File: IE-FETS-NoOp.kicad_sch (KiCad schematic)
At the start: 12 parts, among them Q1 YJG150N03A, Q4 YJG150N03A, U4 INA185A1

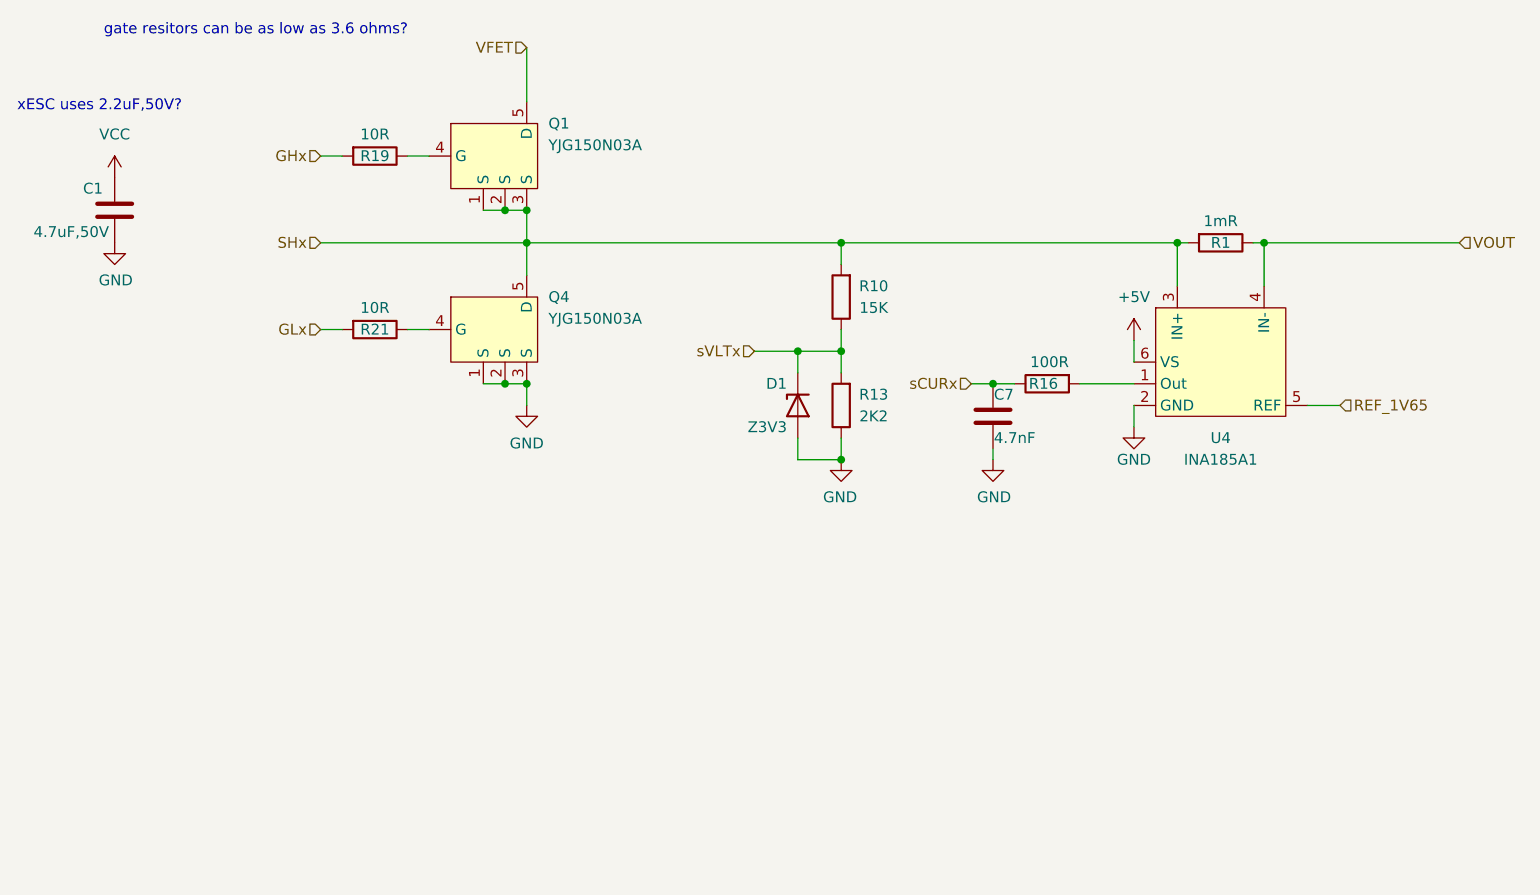
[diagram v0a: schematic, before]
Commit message: push before removing bldc1 external opAmps
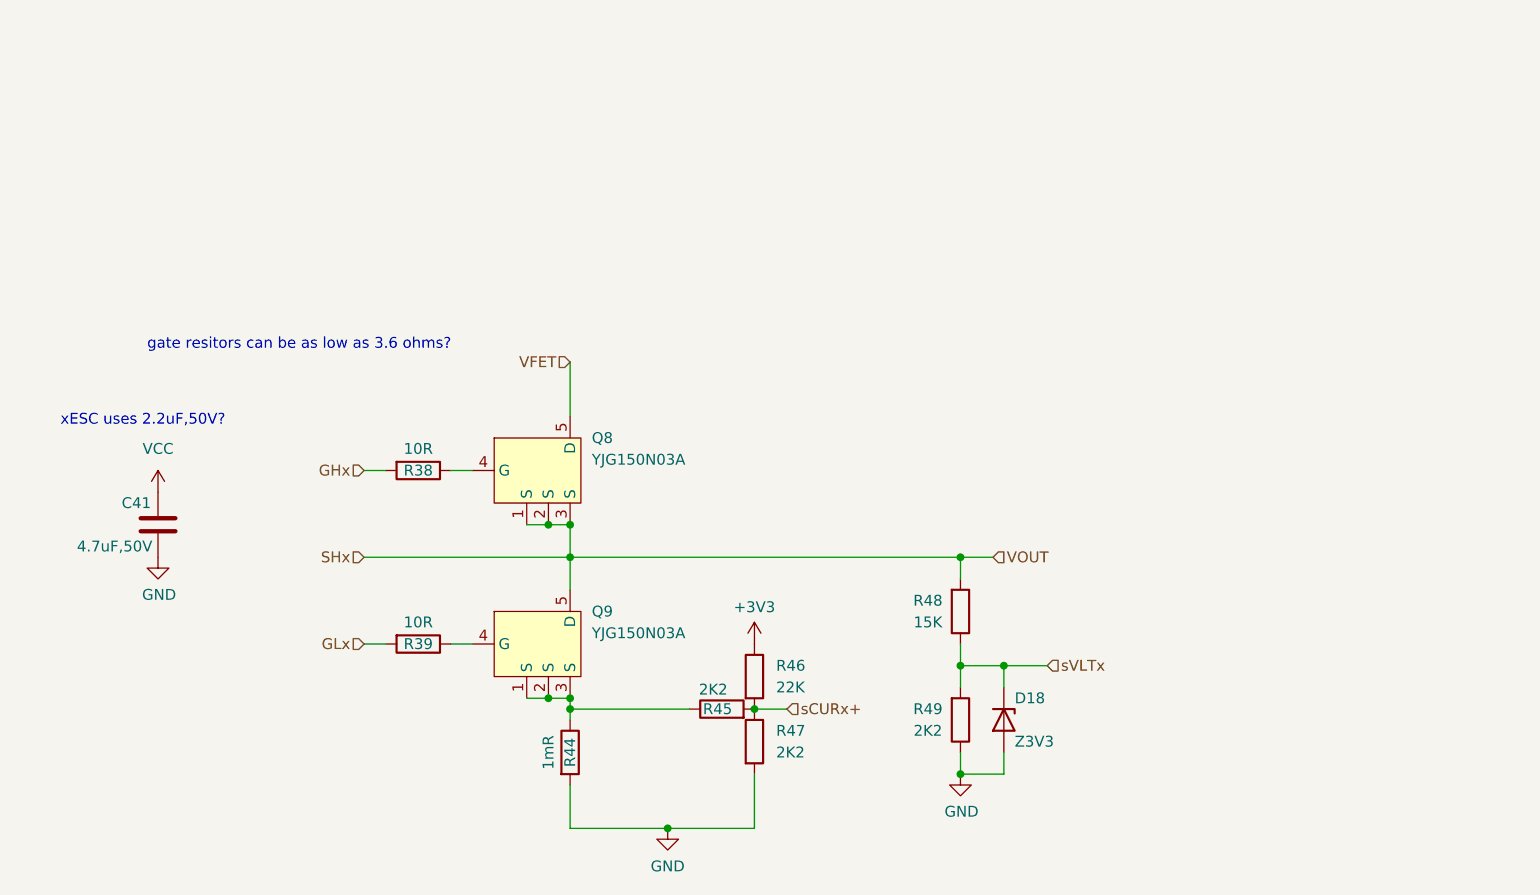
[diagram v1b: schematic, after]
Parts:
- removed C1: 4.7uF,50V, Capacitor_SMD:C_1206_3216Metric, symbol Device:C
- removed C7: 4.7nF, Capacitor_SMD:C_0402_1005Metric, symbol Device:C
- removed D1: Z3V3, Diode_SMD:D_SOD-323_HandSoldering, symbol Device:D_Zener
- removed Q1, Q4: YJG150N03A, Package_TO_SOT_SMD:LFPAK56, symbol AlfredoSymbols:YJG150N03A
- removed R1: 1mR, Resistor_SMD:R_1206_3216Metric, symbol Device:R
- removed R10: 15K, Resistor_SMD:R_0402_1005Metric, symbol Device:R
- removed R13: 2K2, Resistor_SMD:R_0402_1005Metric, symbol Device:R
- removed R16: 100R, Resistor_SMD:R_0402_1005Metric, symbol Device:R
- removed R19, R21: 10R, Resistor_SMD:R_0402_1005Metric, symbol Device:R
- removed U4: INA185A1, Package_TO_SOT_SMD:SOT-563, symbol AlfredoSymbols:INA185A
- added C41: 4.7uF,50V, Capacitor_SMD:C_1206_3216Metric, symbol Device:C
- added D18: Z3V3, Diode_SMD:D_SOD-323_HandSoldering, symbol Device:D_Zener
- added Q8, Q9: YJG150N03A, Package_TO_SOT_SMD:LFPAK56, symbol AlfredoSymbols:YJG150N03A
- added R38, R39: 10R, Resistor_SMD:R_0402_1005Metric, symbol Device:R
- added R44: 1mR, Resistor_SMD:R_1206_3216Metric, symbol Device:R
- added R45, R47, R49: 2K2, Resistor_SMD:R_0402_1005Metric, symbol Device:R
- added R46: 22K, Resistor_SMD:R_0402_1005Metric, symbol Device:R
- added R48: 15K, Resistor_SMD:R_0402_1005Metric, symbol Device:R
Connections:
- net GHx: now also R38.2
- net GLx: now also R39.2
- net GND: now also C41.2, D18.2 (A), R44.2, R47.2, R49.1
- net SHx: now also Q8.1 (S), Q8.2 (S), Q8.3 (S), Q9.5 (D), R48.2
- net VCC: now also C41.1
- net VFET: now also Q8.5 (D)
- net sVLTx: now also D18.1 (K), R48.1, R49.2
- new net: Q9.1 (S), Q9.2 (S), Q9.3 (S), R44.1, R45.1
- new net: Q9.4 (G), R39.1
- new net: Q8.4 (G), R38.1
- new net +3V3: R46.1
- new net sCURx+: R45.2, R46.2, R47.1

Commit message: push for 8/8 order
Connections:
- net VCC is gone; now on net VFET: C41.1
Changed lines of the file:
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@@
+	(hierarchical_label "VFET"
+		(shape input)
+		(at 90.17 88.9 180)
+		(fields_autoplaced yes)
+		(effects
+			(font
+				(size 1.27 1.27)
+			)
+			(justify right)
+		)
+	)
 	(hierarchical_label "VFET"
 		(shape input)
@@
 					(unit 1)
 				)
-			)
-		)
-	)
-	(symbol
-		(lib_id "power:VCC")
-		(at 90.17 88.9 0)
-		(unit 1)
-		(exclude_from_sim no)
-		(in_bom yes)
-		(on_board yes)
-		(dnp no)
-		(fields_autoplaced yes)
-		(property "Reference" "#PWR051"
-			(at 90.17 92.71 0)
-			(effects
-				(font
-					(size 1.27 1.27)
-				)
-				(hide yes)
-			)
-		)
-		(property "Value" "VCC"
-			(at 90.17 83.82 0)
-			(effects
-				(font
-					(size 1.27 1.27)
-				)
-			)
-		)
-		(property "Footprint" ""
-			(at 90.17 88.9 0)
-			(effects
-				(font
-					(size 1.27 1.27)
-				)
-				(hide yes)
-			)
-		)
-		(property "Datasheet" ""
-			(at 90.17 88.9 0)
-			(effects
-				(font
-					(size 1.27 1.27)
-				)
-				(hide yes)
-			)
-		)
-		(property "Description" ""
-			(at 90.17 88.9 0)
-			(effects
-				(font
-					(size 1.27 1.27)
-				)
-				(hide yes)
-			)
-		)
-		(pin "1"
-		)
-		(instances
-			(project "I3ESC"
-				(path "/718f3b0f-9bd0-4d7b-8c07-e00d61b06ce3/3c731236-72d1-4da1-87eb-4e69d9f9de6e"
-					(reference "#PWR051")
-					(unit 1)
-				)
-				(path "/718f3b0f-9bd0-4d7b-8c07-e00d61b06ce3/33fe893d-1f13-49a8-b542-03d4b71301ae"
-					(reference "#PWR056")
-					(unit 1)
-				)
-				(path "/718f3b0f-9bd0-4d7b-8c07-e00d61b06ce3/e04c2199-242b-4a53-bc3f-d16725b8f4ff"
-					(reference "#PWR061")
-					(unit 1)
-				)

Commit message: first push for v2
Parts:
- removed Q8, Q9: YJG150N03A, Package_TO_SOT_SMD:LFPAK56, symbol AlfredoSymbols:YJG150N03A
- removed R38, R39: 10R, Resistor_SMD:R_0402_1005Metric, symbol Device:R
- added R1, R3: 10R, Resistor_SMD:R_0402_1005Metric, symbol Device:R
- added U5: ~, AlfredoFootprints:PQFN8L, symbol AlfredoSymbols:HYG090ND06LS1C2
- C41: value 4.7uF,50V -> 4.7uF, 50V
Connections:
- net GHx: now also R1.2
- net GLx: now also R3.2
- net SHx: now also U5.3 (S2), U5.6 (D1)
- net VFET: now also U5.5 (D2)
- net at R44.1, R45.1: now also U5.1 (S1)
- new net: R1.1, U5.4 (G2)
- new net: R3.1, U5.2 (G1)
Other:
- moved on the sheet: D18, R44, R45, R46, R47, R48, R49
